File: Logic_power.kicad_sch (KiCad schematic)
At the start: 9 parts, among them U2 NJM12877F, U8 L78M05ABDT-TR

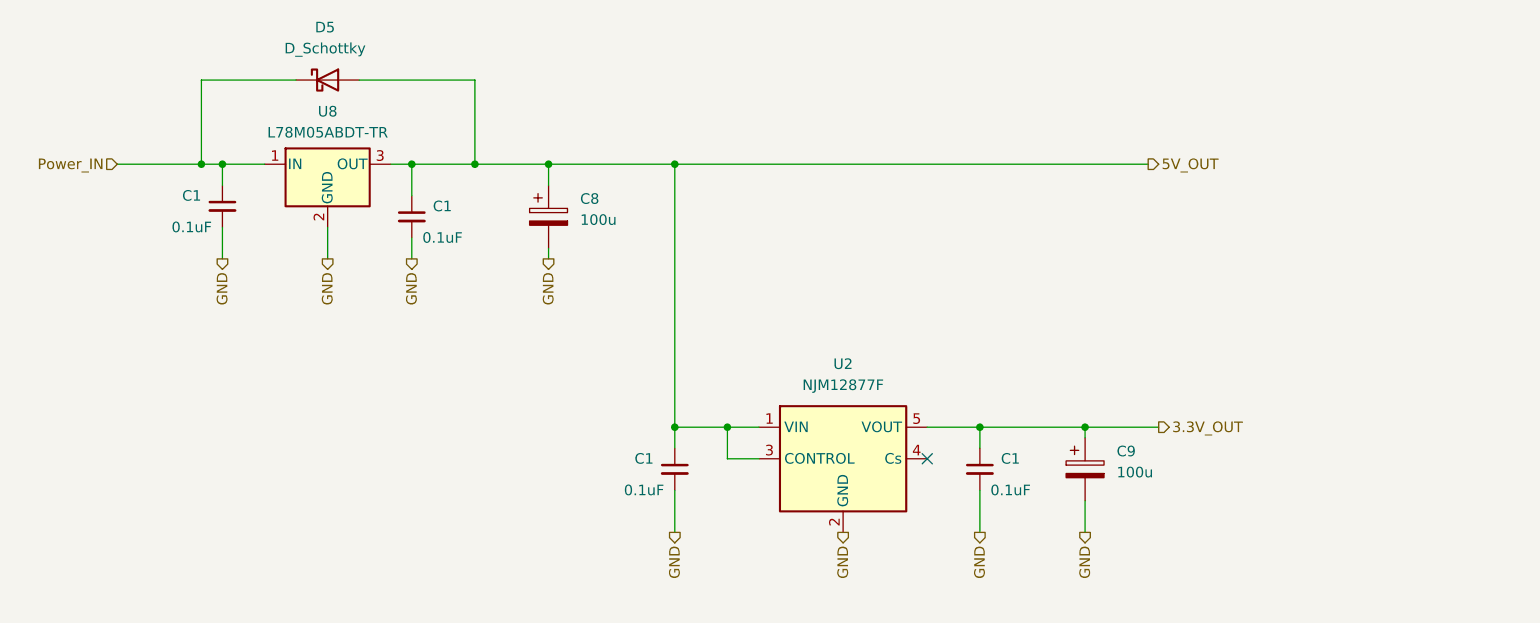
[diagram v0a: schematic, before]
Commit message: update Driver circuit
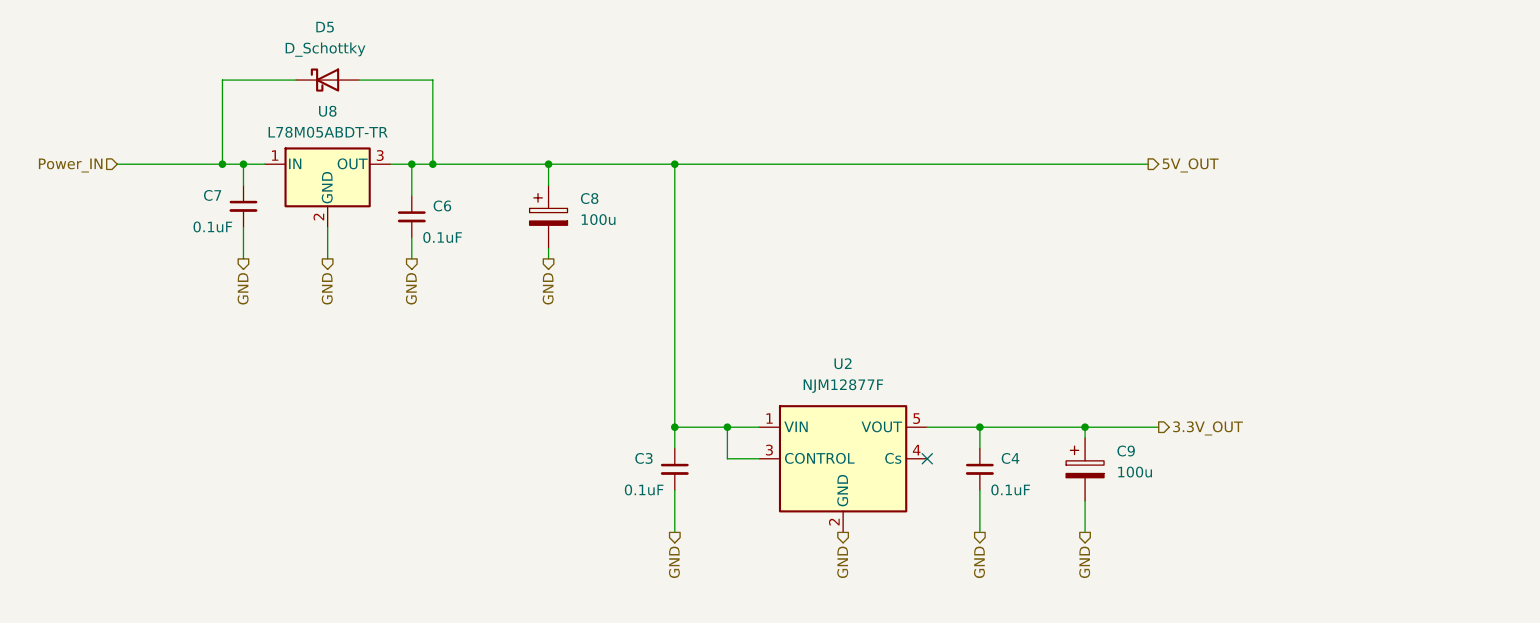
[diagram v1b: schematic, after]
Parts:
- renumbered C1 to C3, C1 to C4, C1 to C6, C1 to C7
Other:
- moved on the sheet: C7
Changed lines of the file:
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@@
   (junction (at 101.6 63.5) (diameter 0) (color 0 0 0 0)
   )
-  (junction (at 38.1 31.75) (diameter 0) (color 0 0 0 0)
-  )
   (junction (at 63.5 31.75) (diameter 0) (color 0 0 0 0)
   )
   (junction (at 95.25 31.75) (diameter 0) (color 0 0 0 0)
   )
+  (junction (at 66.04 31.75) (diameter 0) (color 0 0 0 0)
+  )
   (junction (at 95.25 63.5) (diameter 0) (color 0 0 0 0)
   )
+  (junction (at 144.78 63.5) (diameter 0) (color 0 0 0 0)
+  )
   (junction (at 40.64 31.75) (diameter 0) (color 0 0 0 0)
   )
-  (junction (at 144.78 63.5) (diameter 0) (color 0 0 0 0)
-  )
-  (junction (at 71.12 31.75) (diameter 0) (color 0 0 0 0)
-  )
   (junction (at 80.01 31.75) (diameter 0) (color 0 0 0 0)
   )
+  (junction (at 43.18 31.75) (diameter 0) (color 0 0 0 0)
+  )
   (no_connect (at 125.73 67.31))
-  (wire (pts (xy 40.64 31.75) (xy 40.64 34.29))
+  (wire (pts (xy 43.18 31.75) (xy 45.72 31.75))
+    (stroke (width 0) (type default))
+  )
+  (wire (pts (xy 43.18 31.75) (xy 43.18 34.29))
     (stroke (width 0) (type default))
   )
@@
     (stroke (width 0) (type default))
   )
+  (wire (pts (xy 66.04 31.75) (xy 80.01 31.75))
+    (stroke (width 0) (type default))
+  )
   (wire (pts (xy 132.08 71.12) (xy 132.08 76.2))
     (stroke (width 0) (type default))
@@
     (stroke (width 0) (type default))
   )
-  (wire (pts (xy 57.15 21.59) (xy 71.12 21.59))
+  (wire (pts (xy 57.15 21.59) (xy 66.04 21.59))
     (stroke (width 0) (type default))
   )
@@
     (stroke (width 0) (type default))
   )
-  (wire (pts (xy 40.64 31.75) (xy 45.72 31.75))
+  (wire (pts (xy 27.94 31.75) (xy 40.64 31.75))
     (stroke (width 0) (type default))
   )
@@
     (stroke (width 0) (type default))
   )
-  (wire (pts (xy 71.12 21.59) (xy 71.12 31.75))
+  (wire (pts (xy 66.04 21.59) (xy 66.04 31.75))
     (stroke (width 0) (type default))
   )
@@
     (stroke (width 0) (type default))
   )
-  (wire (pts (xy 27.94 31.75) (xy 38.1 31.75))
-    (stroke (width 0) (type default))
-  )
   (wire (pts (xy 95.25 31.75) (xy 152.4 31.75))
     (stroke (width 0) (type default))
@@
     (stroke (width 0) (type default))
   )
-  (wire (pts (xy 63.5 31.75) (xy 71.12 31.75))
+  (wire (pts (xy 63.5 31.75) (xy 66.04 31.75))
     (stroke (width 0) (type default))
   )
@@
     (stroke (width 0) (type default))
   )
+  (wire (pts (xy 40.64 31.75) (xy 43.18 31.75))
+    (stroke (width 0) (type default))
+  )
   (wire (pts (xy 63.5 40.64) (xy 63.5 43.18))
     (stroke (width 0) (type default))
@@
     (stroke (width 0) (type default))
   )
-  (wire (pts (xy 71.12 31.75) (xy 80.01 31.75))
-    (stroke (width 0) (type default))
-  )
   (wire (pts (xy 105.41 63.5) (xy 101.6 63.5))
     (stroke (width 0) (type default))
   )
-  (wire (pts (xy 40.64 39.37) (xy 40.64 43.18))
-    (stroke (width 0) (type default))
-  )
-  (wire (pts (xy 38.1 21.59) (xy 38.1 31.75))
-    (stroke (width 0) (type default))
-  )
-  (wire (pts (xy 38.1 31.75) (xy 40.64 31.75))
-    (stroke (width 0) (type default))
-  )
-  (wire (pts (xy 49.53 21.59) (xy 38.1 21.59))
+  (wire (pts (xy 43.18 39.37) (xy 43.18 43.18))
+    (stroke (width 0) (type default))
+  )
+  (wire (pts (xy 40.64 21.59) (xy 40.64 31.75))
+    (stroke (width 0) (type default))
+  )
+  (wire (pts (xy 49.53 21.59) (xy 40.64 21.59))
     (stroke (width 0) (type default))
   )
@@
     (effects (font (size 1.27 1.27)) (justify left))
   )
-  (hierarchical_label "GND" (shape output) (at 40.64 43.18 270) (fields_autoplaced)
+  (hierarchical_label "GND" (shape output) (at 43.18 43.18 270) (fields_autoplaced)
     (effects (font (size 1.27 1.27)) (justify right))
   )
@@
     )
   )
-  (symbol (lib_id "Device:C_Small") (at 40.64 36.83 0) (unit 1)
+  (symbol (lib_id "Device:C_Small") (at 43.18 36.83 0) (unit 1)
     (in_bom yes) (on_board yes) (dnp no)
-    (property "Reference" "C1" (at 38.1 35.5663 0)
-      (effects (font (size 1.27 1.27)) (justify right))
-    )
-    (property "Value" "0.1uF" (at 39.37 39.37 0)
-      (effects (font (size 1.27 1.27)) (justify right))
-    )
-    (property "Footprint" "" (at 40.64 36.83 0)
-      (effects (font (size 1.27 1.27)) hide)
-    )
-    (property "Datasheet" "~" (at 40.64 36.83 0)
-      (effects (font (size 1.27 1.27)) hide)
-    )
-    (pin "2")
-    (pin "1")
-    (instances
-      (project "schematic_MD"
-        (path "/3152684b-d11f-4a9a-8e6c-09965044adbd"
-          (reference "C1") (unit 1)
-        )
-        (path "/3152684b-d11f-4a9a-8e6c-09965044adbd/878f32b7-0d3d-4f49-a9dc-ebc0f2e1c793"
-          (reference "C29") (unit 1)
-        )
+    (property "Reference" "C7" (at 40.64 35.5663 0)
+      (effects (font (size 1.27 1.27)) (justify right))
+    )
+    (property "Value" "0.1uF" (at 41.91 39.37 0)
+      (effects (font (size 1.27 1.27)) (justify right))
+    )
+    (property "Footprint" "" (at 43.18 36.83 0)
+      (effects (font (size 1.27 1.27)) hide)
+    )
+    (property "Datasheet" "~" (at 43.18 36.83 0)
+      (effects (font (size 1.27 1.27)) hide)
+    )
+    (pin "2")
+    (pin "1")
+    (instances
+      (project "schematic_MD"
         (path "/3152684b-d11f-4a9a-8e6c-09965044adbd/2d267caf-42fc-44ea-97db-65c2b77a1587"
           (reference "C7") (unit 1)
@@
   (symbol (lib_id "Device:C_Small") (at 132.08 68.58 0) (mirror y) (unit 1)
     (in_bom yes) (on_board yes) (dnp no)
-    (property "Reference" "C1" (at 134.62 67.3163 0)
+    (property "Reference" "C4" (at 134.62 67.3163 0)
       (effects (font (size 1.27 1.27)) (justify right))
     )
@@
     (instances
       (project "schematic_MD"
-        (path "/3152684b-d11f-4a9a-8e6c-09965044adbd"
-          (reference "C1") (unit 1)
-        )
-        (path "/3152684b-d11f-4a9a-8e6c-09965044adbd/878f32b7-0d3d-4f49-a9dc-ebc0f2e1c793"
-          (reference "C29") (unit 1)
-        )
         (path "/3152684b-d11f-4a9a-8e6c-09965044adbd/2d267caf-42fc-44ea-97db-65c2b77a1587"
           (reference "C4") (unit 1)
@@
   (symbol (lib_id "Device:C_Small") (at 63.5 38.1 0) (mirror y) (unit 1)
     (in_bom yes) (on_board yes) (dnp no)
-    (property "Reference" "C1" (at 66.04 36.8363 0)
+    (property "Reference" "C6" (at 66.04 36.8363 0)
       (effects (font (size 1.27 1.27)) (justify right))
     )
@@
     (instances
       (project "schematic_MD"
-        (path "/3152684b-d11f-4a9a-8e6c-09965044adbd"
-          (reference "C1") (unit 1)
-        )
-        (path "/3152684b-d11f-4a9a-8e6c-09965044adbd/878f32b7-0d3d-4f49-a9dc-ebc0f2e1c793"
-          (reference "C29") (unit 1)
-        )
         (path "/3152684b-d11f-4a9a-8e6c-09965044adbd/2d267caf-42fc-44ea-97db-65c2b77a1587"
           (reference "C6") (unit 1)
@@
   (symbol (lib_id "Device:C_Small") (at 95.25 68.58 0) (unit 1)
     (in_bom yes) (on_board yes) (dnp no)
-    (property "Reference" "C1" (at 92.71 67.3163 0)
+    (property "Reference" "C3" (at 92.71 67.3163 0)
       (effects (font (size 1.27 1.27)) (justify right))
     )
@@
     (instances
       (project "schematic_MD"
-        (path "/3152684b-d11f-4a9a-8e6c-09965044adbd"
-          (reference "C1") (unit 1)
-        )
-        (path "/3152684b-d11f-4a9a-8e6c-09965044adbd/878f32b7-0d3d-4f49-a9dc-ebc0f2e1c793"
-          (reference "C29") (unit 1)
-        )
         (path "/3152684b-d11f-4a9a-8e6c-09965044adbd/2d267caf-42fc-44ea-97db-65c2b77a1587"
           (reference "C3") (unit 1)

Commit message: add footprint
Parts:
- C3, C4, C6, C7: value 0.1uF -> 0.1u
- C8, C9: footprint (none) -> Capacitor_THT:CP_Radial_D6.3mm_P2.50mm
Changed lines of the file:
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@@
       (effects (font (size 1.27 1.27)) (justify left))
     )
-    (property "Footprint" "" (at 80.9752 41.91 0)
+    (property "Footprint" "Capacitor_THT:CP_Radial_D6.3mm_P2.50mm" (at 80.9752 41.91 0)
       (effects (font (size 1.27 1.27)) hide)
     )
@@
       (effects (font (size 1.27 1.27)) (justify right))
     )
-    (property "Value" "0.1uF" (at 41.91 39.37 0)
+    (property "Value" "0.1u" (at 41.91 39.37 0)
       (effects (font (size 1.27 1.27)) (justify right))
     )
@@
       (effects (font (size 1.27 1.27)) (justify right))
     )
-    (property "Value" "0.1uF" (at 133.35 71.12 0)
+    (property "Value" "0.1u" (at 133.35 71.12 0)
       (effects (font (size 1.27 1.27)) (justify right))
     )
@@
       (effects (font (size 1.27 1.27)) (justify right))
     )
-    (property "Value" "0.1uF" (at 64.77 40.64 0)
+    (property "Value" "0.1u" (at 64.77 40.64 0)
       (effects (font (size 1.27 1.27)) (justify right))
     )
@@
       (effects (font (size 1.27 1.27)) (justify left))
     )
-    (property "Footprint" "" (at 145.7452 72.39 0)
+    (property "Footprint" "Capacitor_THT:CP_Radial_D6.3mm_P2.50mm" (at 145.7452 72.39 0)
       (effects (font (size 1.27 1.27)) hide)
     )
@@
       (effects (font (size 1.27 1.27)) (justify right))
     )
-    (property "Value" "0.1uF" (at 93.98 71.12 0)
+    (property "Value" "0.1u" (at 93.98 71.12 0)
       (effects (font (size 1.27 1.27)) (justify right))
     )

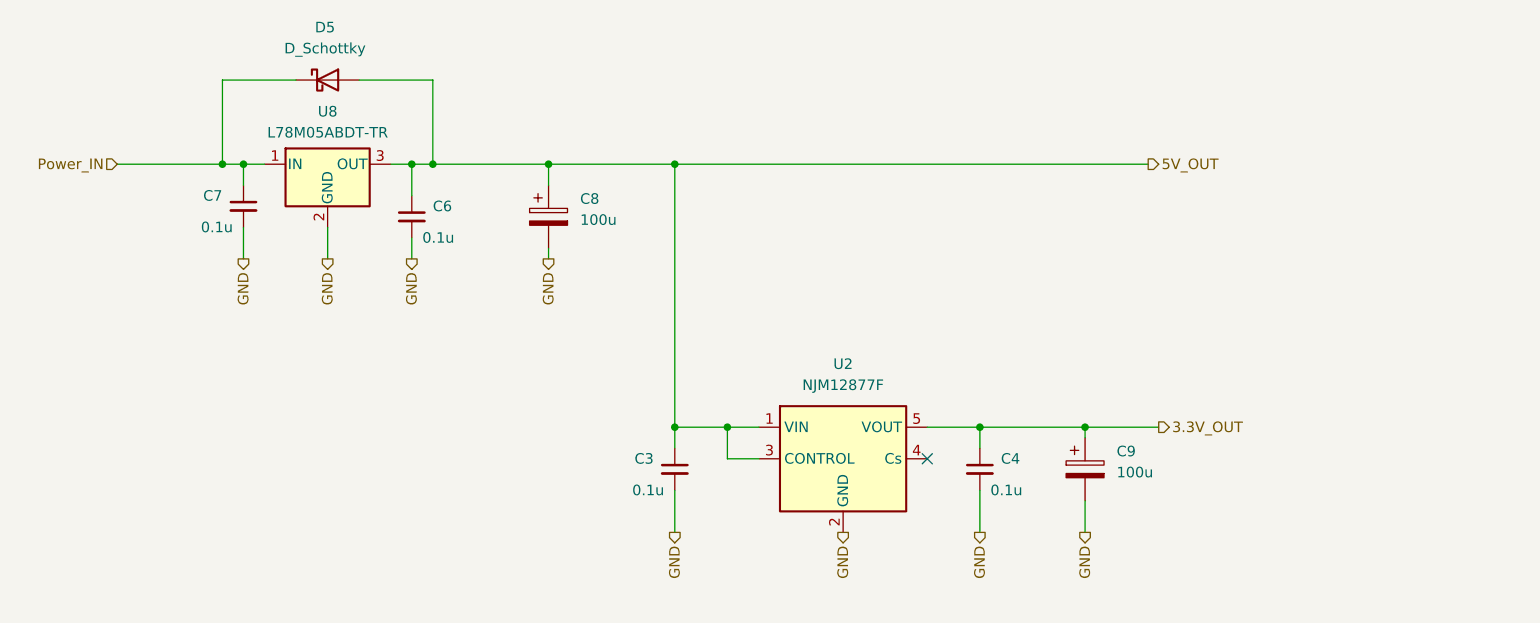
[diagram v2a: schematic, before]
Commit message: Update motor driver circuit
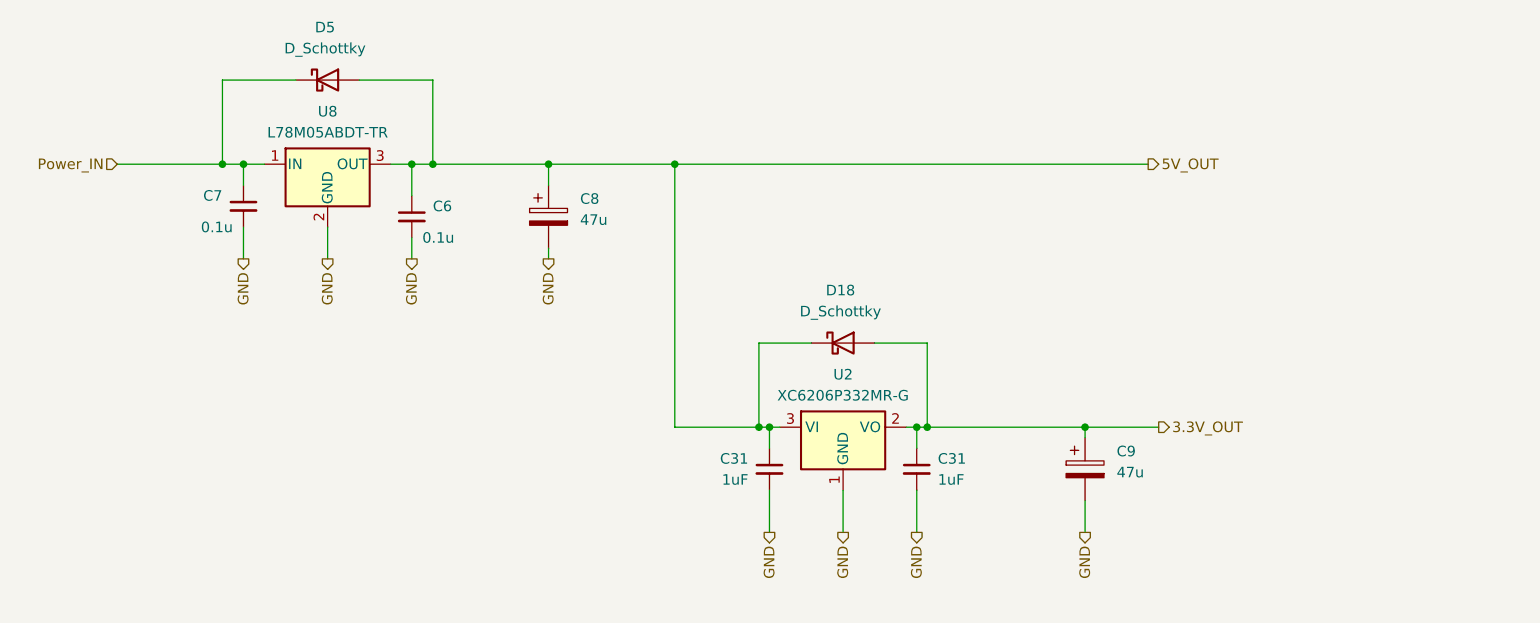
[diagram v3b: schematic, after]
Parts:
- removed C3, C4: 0.1u, symbol Device:C_Small
- removed U2: NJM12877F, Package_TO_SOT_SMD:SOT-23-5, symbol RDC_generic:NJM12877F
- added C31 (x2): 1uF, Capacitor_SMD:C_0603_1608Metric_Pad1.08x0.95mm_HandSolder, symbol Device:C_Small
- added D18: D_Schottky, Diode_SMD:D_SOD-123F, symbol Device:D_Schottky
- added U2: XC6206P332MR-G, Package_TO_SOT_SMD:SOT-23-3, symbol RDC_generic:XC6206P332MR-G
- C6, C7: footprint (none) -> Capacitor_SMD:C_0603_1608Metric_Pad1.08x0.95mm_HandSolder
- C8, C9: value 100u -> 47u; footprint Capacitor_THT:CP_Radial_D6.3mm_P2.50mm -> Capacitor_THT:CP_Radial_D5.0mm_P2.00mm
- D5: footprint (none) -> Diode_SMD:D_SOD-123F
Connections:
- net 3.3V_OUT: now also C31.1, D18.2 (A), U2.2 (VO)
- net 5V_OUT: now also C31.1, D18.1 (K), U2.3 (VI)
- net GND: now also C31.2, C31.2, U2.1 (GND)
- no-connect marks 1 -> 0

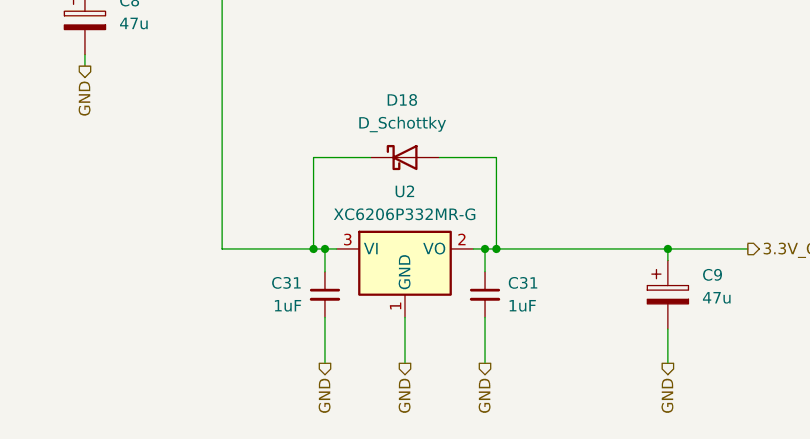
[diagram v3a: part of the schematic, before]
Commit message: add MOSFET pulldown
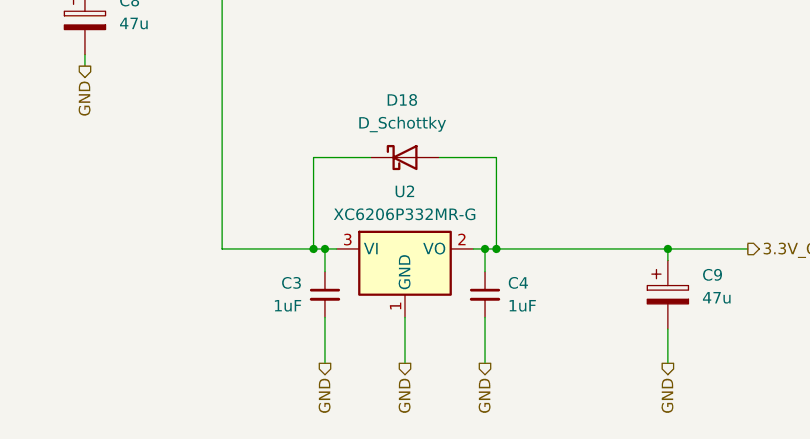
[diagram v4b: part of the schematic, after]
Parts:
- renumbered C31 to C3, C31 to C4
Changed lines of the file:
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@@
   (symbol (lib_id "Device:C_Small") (at 124.46 68.58 0) (mirror y) (unit 1)
     (in_bom yes) (on_board yes) (dnp no)
-    (property "Reference" "C31" (at 127 67.3163 0)
+    (property "Reference" "C4" (at 127 67.3163 0)
       (effects (font (size 1.27 1.27)) (justify right))
     )
@@
     (instances
       (project "schematic_MD"
-        (path "/3152684b-d11f-4a9a-8e6c-09965044adbd/878f32b7-0d3d-4f49-a9dc-ebc0f2e1c793"
-          (reference "C31") (unit 1)
-        )
         (path "/3152684b-d11f-4a9a-8e6c-09965044adbd/2d267caf-42fc-44ea-97db-65c2b77a1587"
           (reference "C4") (unit 1)
@@
   (symbol (lib_id "Device:C_Small") (at 106.68 68.58 0) (unit 1)
     (in_bom yes) (on_board yes) (dnp no)
-    (property "Reference" "C31" (at 104.14 67.3163 0)
+    (property "Reference" "C3" (at 104.14 67.3163 0)
       (effects (font (size 1.27 1.27)) (justify right))
     )
@@
     (instances
       (project "schematic_MD"
-        (path "/3152684b-d11f-4a9a-8e6c-09965044adbd/878f32b7-0d3d-4f49-a9dc-ebc0f2e1c793"
-          (reference "C31") (unit 1)
-        )
         (path "/3152684b-d11f-4a9a-8e6c-09965044adbd/2d267caf-42fc-44ea-97db-65c2b77a1587"
           (reference "C3") (unit 1)

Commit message: add branch v0.2.0
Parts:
- removed C8, C9: 47u, Capacitor_THT:CP_Radial_D5.0mm_P2.00mm, symbol Device:C_Polarized
- removed D5: D_Schottky, Diode_SMD:D_SOD-123F, symbol Device:D_Schottky
- removed U8: L78M05ABDT-TR, Package_TO_SOT_SMD:TO-252-2, symbol RDC_generic:L78M05ABDT-TR
- added C41: 10u, Capacitor_SMD:C_0603_1608Metric_Pad1.08x0.95mm_HandSolder, symbol Device:C_Small
- added C42: 22u, Capacitor_SMD:C_0603_1608Metric_Pad1.08x0.95mm_HandSolder, symbol Device:C_Small
- added C62: 0.1u, Capacitor_SMD:C_0603_1608Metric_Pad1.08x0.95mm_HandSolder, symbol Device:C_Small
- added L1: 15uH, symbol Device:L_Iron
- added U10: TPS54202DDC, Package_TO_SOT_SMD:SOT-23-6, symbol Regulator_Switching:TPS54202DDC
- C6: value 0.1u -> 22u
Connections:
- net 5V_OUT: now also C42.1, C62.2, L1.2
- net GND: now also C41.2, C42.2, U10.1 (GND)
- net Power_IN: now also C41.1, U10.3 (VIN)
- new net: C62.1, U10.6 (BOOT)
- new net: L1.1, U10.2 (SW)
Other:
- moved on the sheet: C3, C4, C6, C7, D18, U2
